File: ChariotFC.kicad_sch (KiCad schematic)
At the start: 49 parts, among them SW1 1TS009A-1800-5000, SW2 1TS009A-1800-5000, U1 AT32F435RMT7, U2 FM25V20A-DGTR_C2952834, U3 NCP167BMX330TBG, U4 TLV75733PDRVR, U5 B6B-XH-A(LF)(SN), U6 USBLC6-2SC6Y_C2969755, X1 ABM3-8.000MHZ-D2Y-T

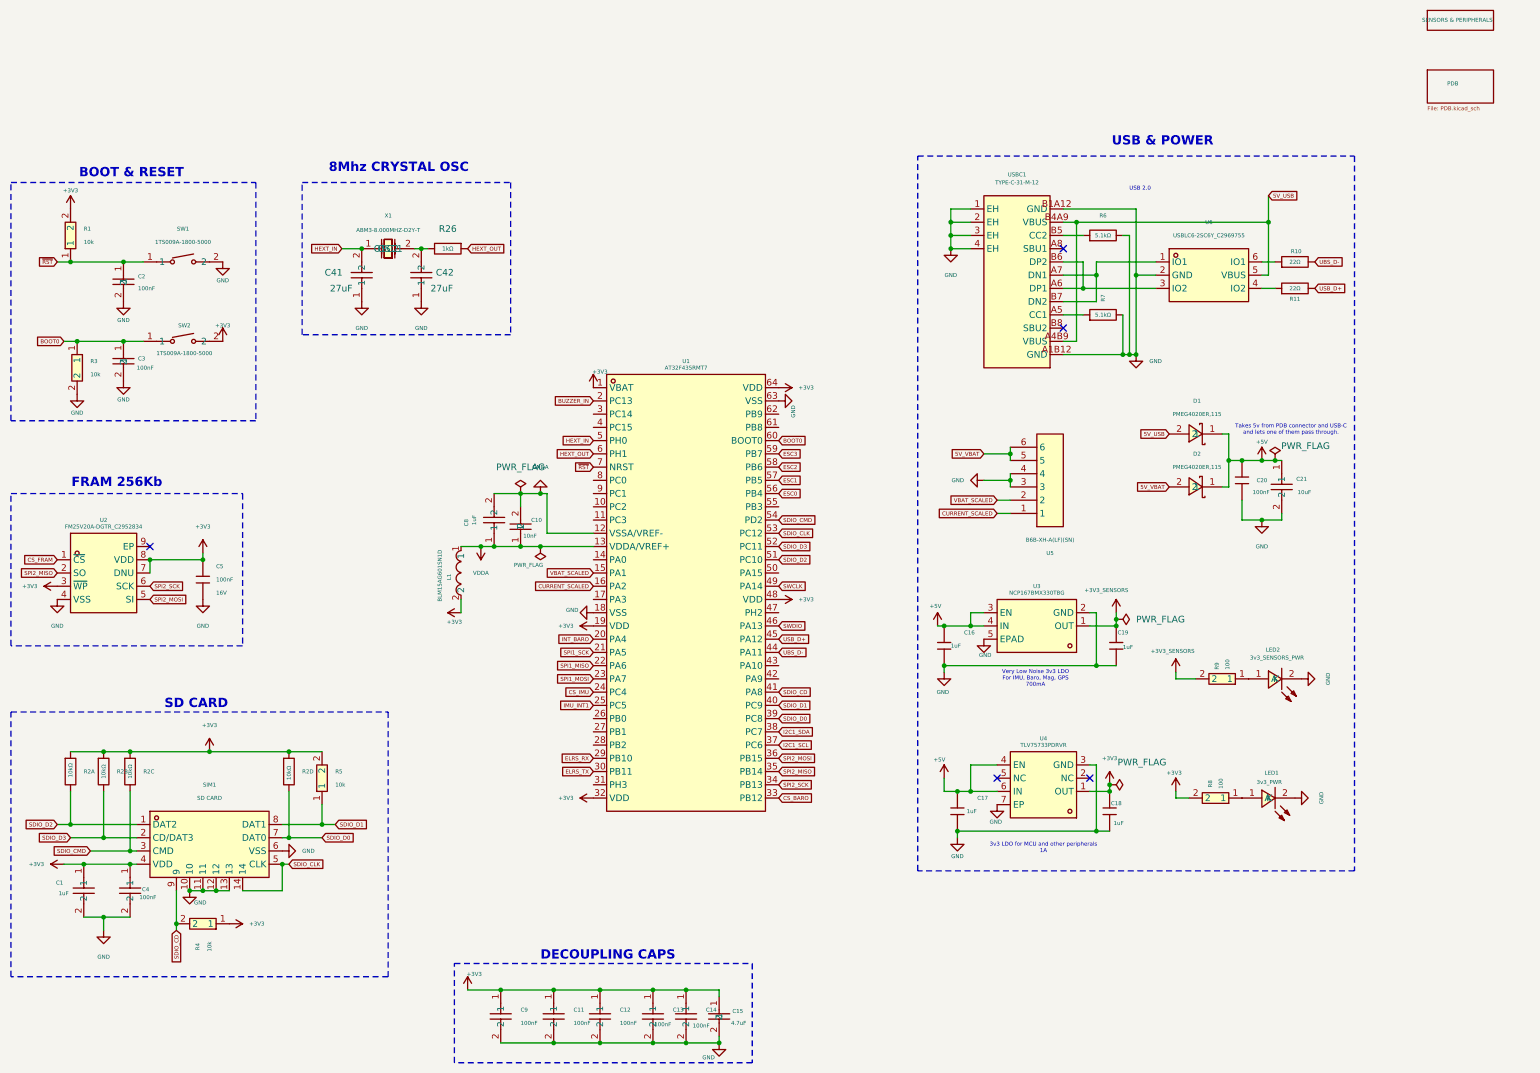
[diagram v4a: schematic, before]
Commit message: Assigned proper footprints, Re-annotated, Connection modification for efficient PCB layout, First PCB update
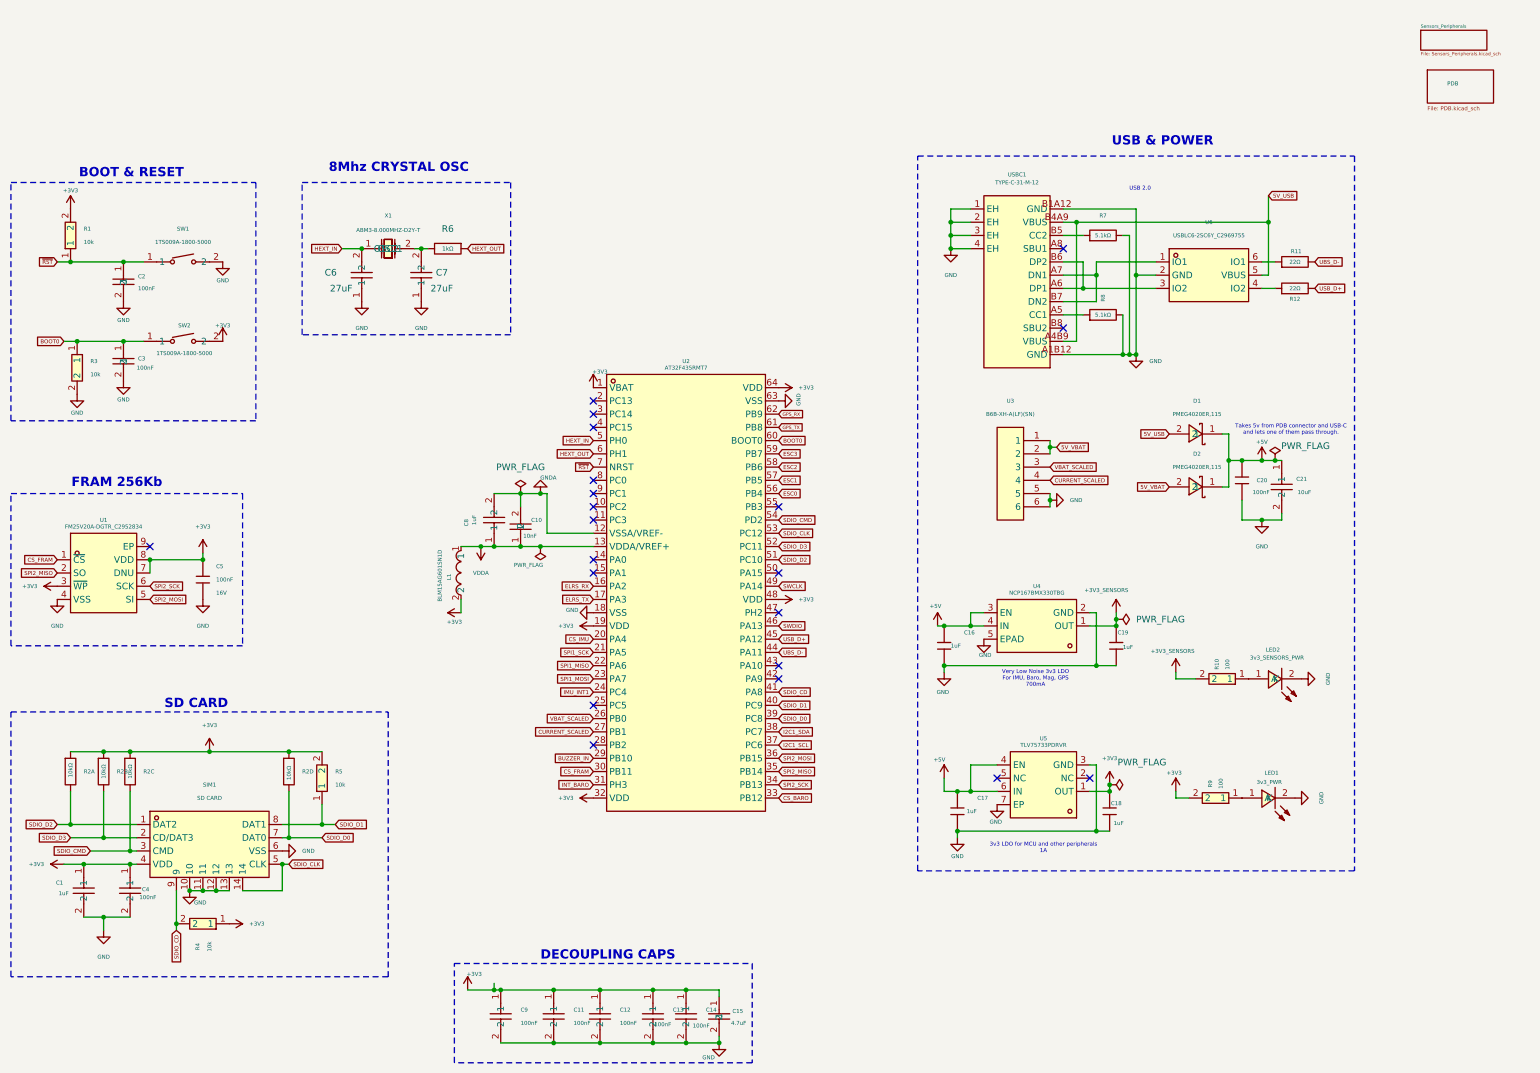
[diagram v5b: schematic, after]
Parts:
- C16, C17, C18, C19, C20, C5: footprint PCM_JLCPCB:C_0402 -> easyeda2kicad:C0402
- R11: renamed from R10; footprint PCM_JLCPCB:R_0402 -> easyeda2kicad:R0402
- R12: renamed from R11; footprint PCM_JLCPCB:R_0402 -> easyeda2kicad:R0402
- R2: footprint PCM_JLCPCB:R_0402x4 -> easyeda2kicad:RES-ARRAY-SMD_0402-8P-L2.0-W1.0-BL
- R6: renamed from R26; footprint PCM_JLCPCB:R_0402 -> easyeda2kicad:R0402
- R7: renamed from R6; footprint PCM_JLCPCB:R_0402 -> easyeda2kicad:R0402
- R8: renamed from R7; footprint PCM_JLCPCB:R_0402 -> easyeda2kicad:R0402
- renumbered C41 to C6, C42 to C7, R9 to R10, R8 to R9, U2 to U1, U1 to U2, U5 to U3, U3 to U4, U4 to U5
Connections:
- net 5V_VBAT: now also U3.1, U3.2; no longer U3.5, U3.6
- net BUZZER_IN: now also U2.29 (PB10); no longer U2.2 (PC13)
- net CS_FRAM: now also U2.30 (PB11)
- net CS_IMU: now also U2.20 (PA4); no longer U2.24 (PC4)
- net CURRENT_SCALED: now also U2.27 (PB1), U3.4; no longer U2.16 (PA2), U3.1
- net ELRS_RX: now also U2.16 (PA2); no longer U2.29 (PB10)
- net ELRS_TX: now also U2.17 (PA3); no longer U2.30 (PB11)
- net GND: now also U3.5, U3.6; no longer U3.3, U3.4
- net IMU_INT1: now also U2.24 (PC4); no longer U2.25 (PC5)
- net INT_BARO: now also U2.31 (PH3); no longer U2.20 (PA4)
- net VBAT_SCALED: now also U2.26 (PB0), U3.3; no longer U2.15 (PA1), U3.2
- net GPS_TX: now reaches U2.61 (PB8)
- net GPS_RX: now reaches U2.62 (PB9)
- no-connect marks 5 -> 21
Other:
- removed sheet SENSORS & PERIPHERALS
- added sheet Sensors_Peripherals (Sensors_Peripherals.kicad_sch)
- moved on the sheet: U3
